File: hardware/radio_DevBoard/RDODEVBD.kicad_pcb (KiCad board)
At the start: 2 copper layers, 21 parts, among them J1 SMA, P1 CONN_01X08, U1 AX5043, X1 CRYSTAL_SMD

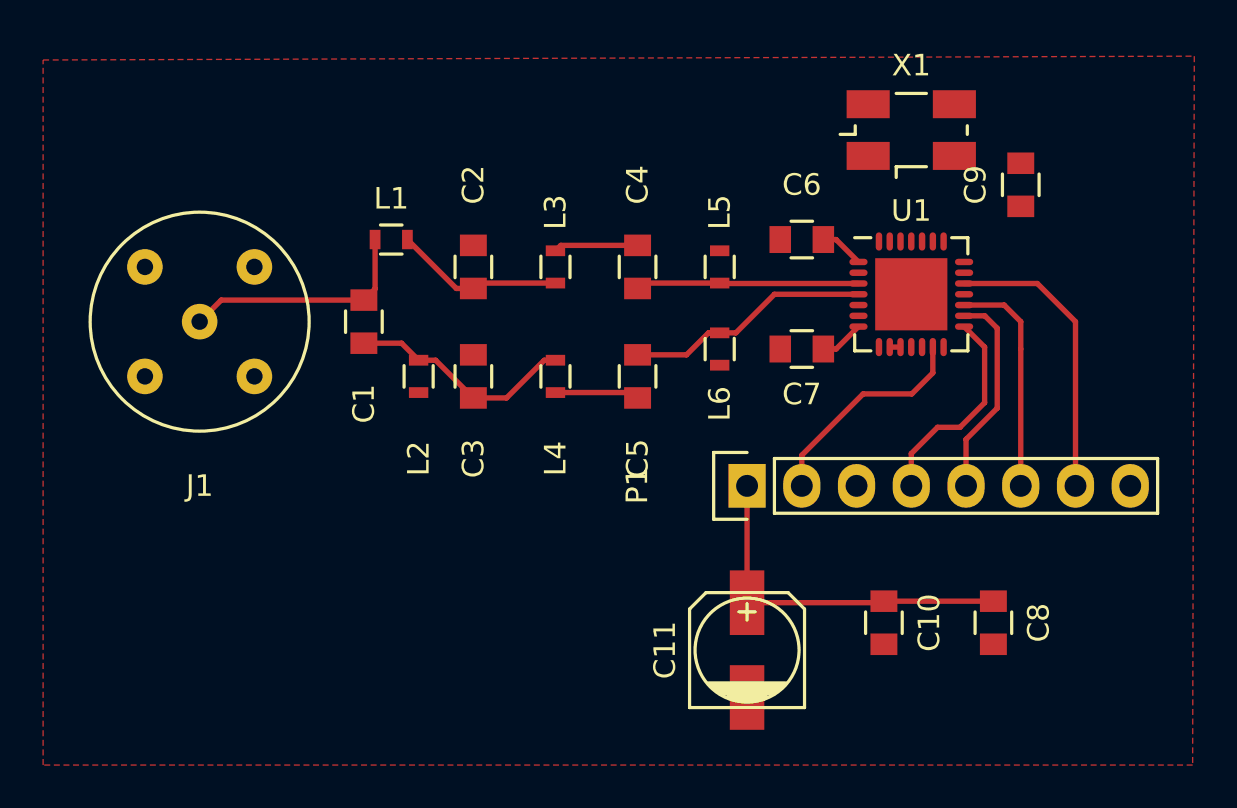
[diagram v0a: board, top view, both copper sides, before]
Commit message: Finished Radio Interface Dev & Audio Dev Schematic
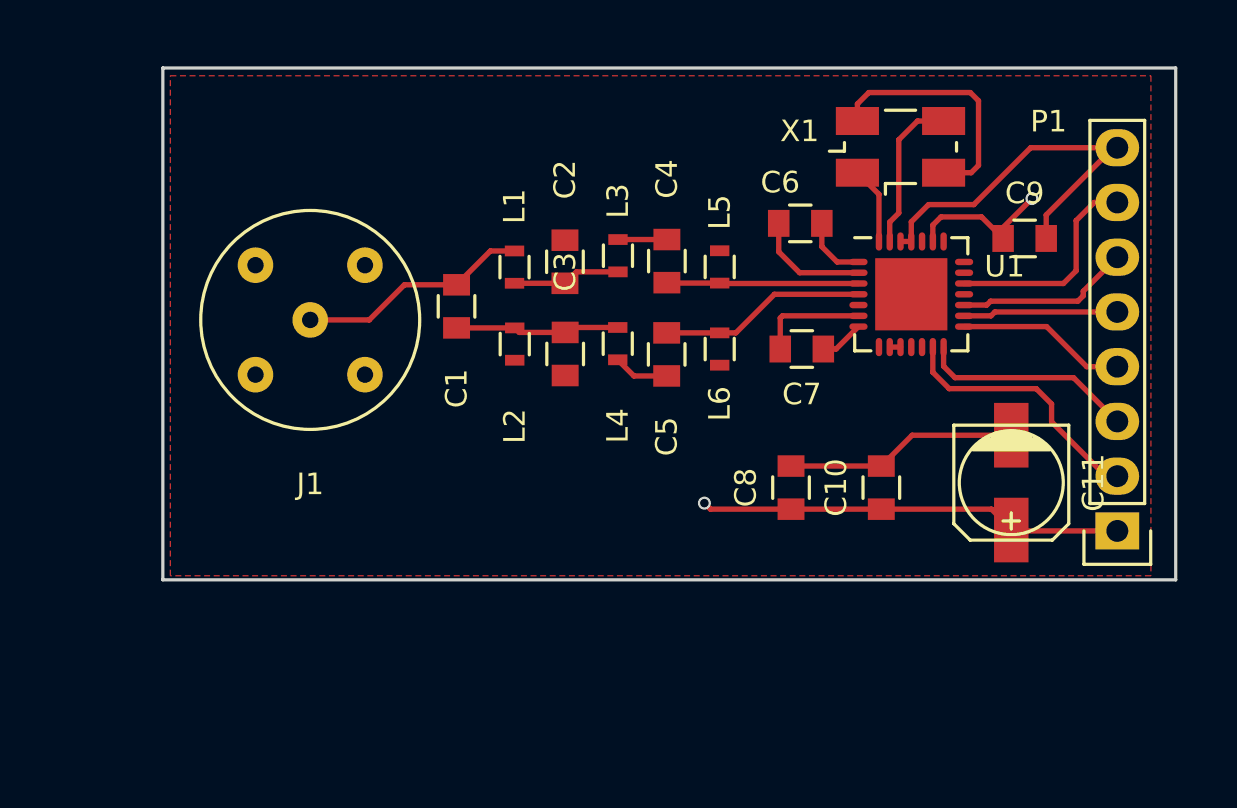
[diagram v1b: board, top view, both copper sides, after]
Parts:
- moved P1 17.3 mm to (135.3, 106.2), turned to 180 degrees
- moved C11 14.5 mm to (130.4, 104.0), turned to 270 degrees
- moved C8 11.3 mm to (120.2, 104.2), turned to 90 degrees
- moved C10 6.27 mm to (124.3, 104.2), turned to 90 degrees
- moved L1 5.86 mm to (107.3, 94.0), turned to 270 degrees
- moved J1 5.13 mm to (97.8, 96.4)
- moved L2 4.71 mm to (107.3, 97.6)
- moved C3 4.39 mm to (109.7, 98.0), turned to 90 degrees
- moved C1 4.36 mm to (104.6, 95.8)
- moved C2 4.26 mm to (109.7, 93.7)
- moved L4 3.27 mm to (112.1, 97.5)
- moved L3 2.95 mm to (112.1, 93.5)
- moved C9 2.50 mm to (131.0, 92.7), turned to 0 degrees
- moved C5 1.69 mm to (114.4, 98.0)
- moved C4 1.39 mm to (114.4, 93.7)
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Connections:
- C2 pad 1: Net-(C2-Pad1) -> GND
- C6 pad 2: Net-(C2-Pad1) -> GND
- L5 pad 1: Net-(C2-Pad1) -> GND
- P1 pad 3: SEL -> ~SEL
- U1 pad 2: Net-(C2-Pad1) -> GND
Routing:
- net GND: track 0.00 -> 39.4 mm
- net Net-(X1-Pad3): track 0.00 -> 11.5 mm
- net ~SEL: track 0.00 -> 10.0 mm
- net VDD: track 17.0 -> 26.7 mm, vias 0 -> 2
- net Net-(U1-Pad27): track 0.00 -> 7.33 mm
- net Net-(U1-Pad28): track 0.00 -> 3.60 mm
- net IRQ: track 13.5 -> 10.0 mm
- net Net-(C1-Pad1): track 10.7 -> 7.66 mm
- net Net-(C2-Pad2): track 7.91 -> 5.02 mm
- net MISO: track 9.69 -> 7.18 mm
- net MOSI: track 10.6 -> 8.15 mm
- net SYSCLK: track 10.3 -> 12.2 mm
- net CLK: track 9.80 -> 7.88 mm
- net Net-(C5-Pad1): track 11.4 -> 9.64 mm
- net Net-(C4-Pad2): track 3.91 -> 2.27 mm
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- added copper zone on In1.Cu, net GND
- added copper zone on In2.Cu, net VDD
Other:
- board outline added: 47 x 23.8 mm
- copper layers 2 -> 4
